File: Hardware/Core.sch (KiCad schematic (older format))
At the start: 24 parts, among them U1 AAT1217

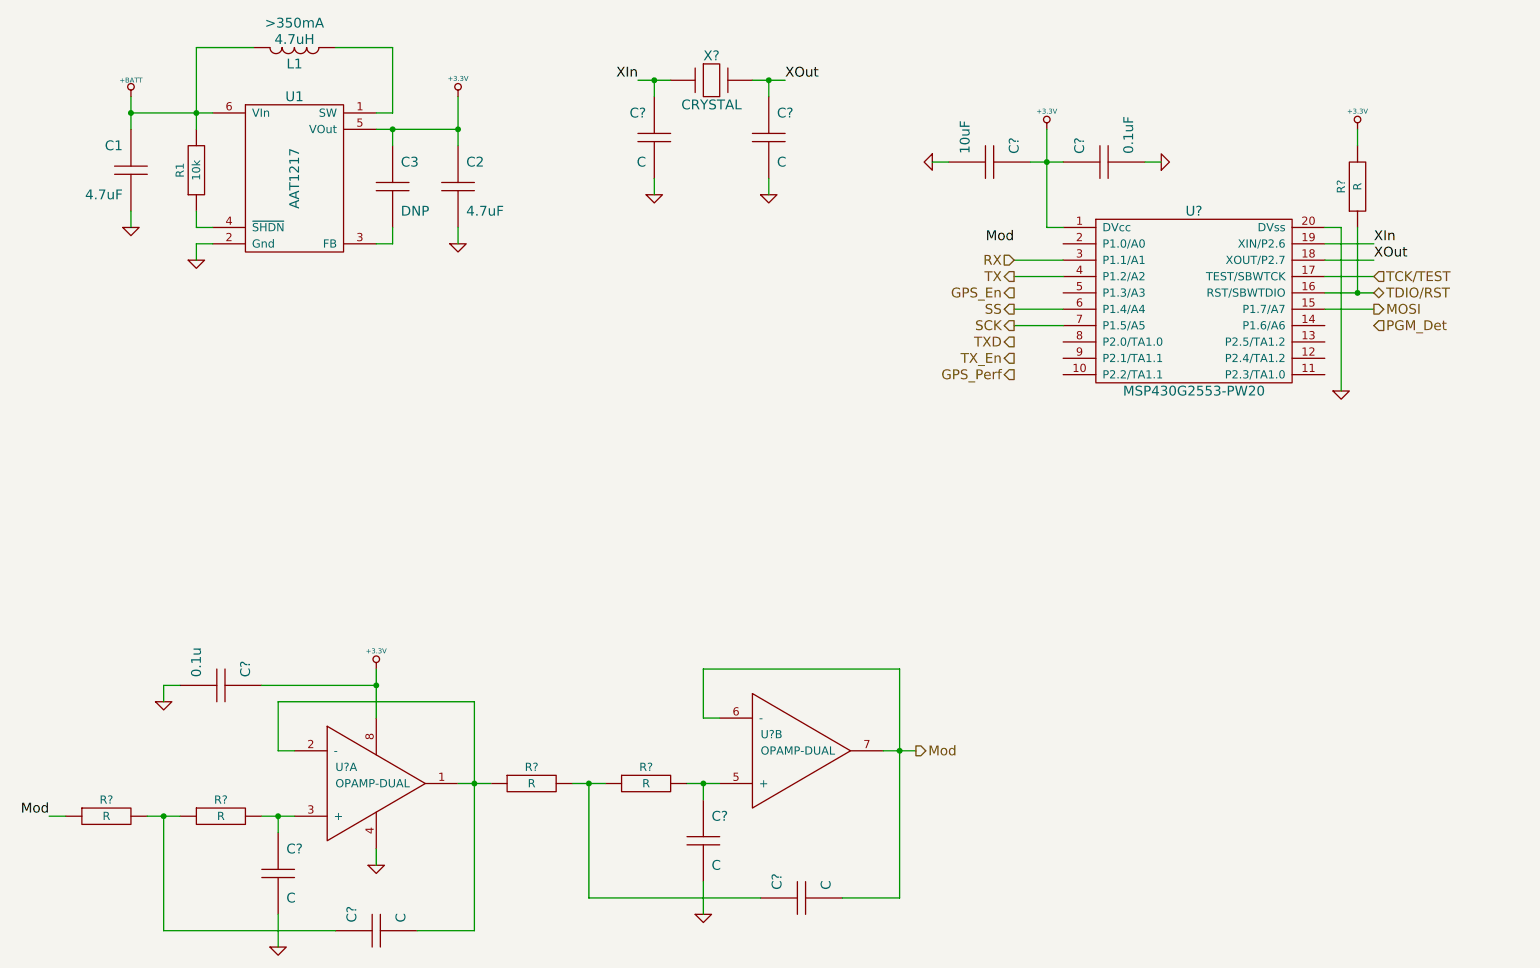
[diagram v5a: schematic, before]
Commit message: Change to 28 pin MCU
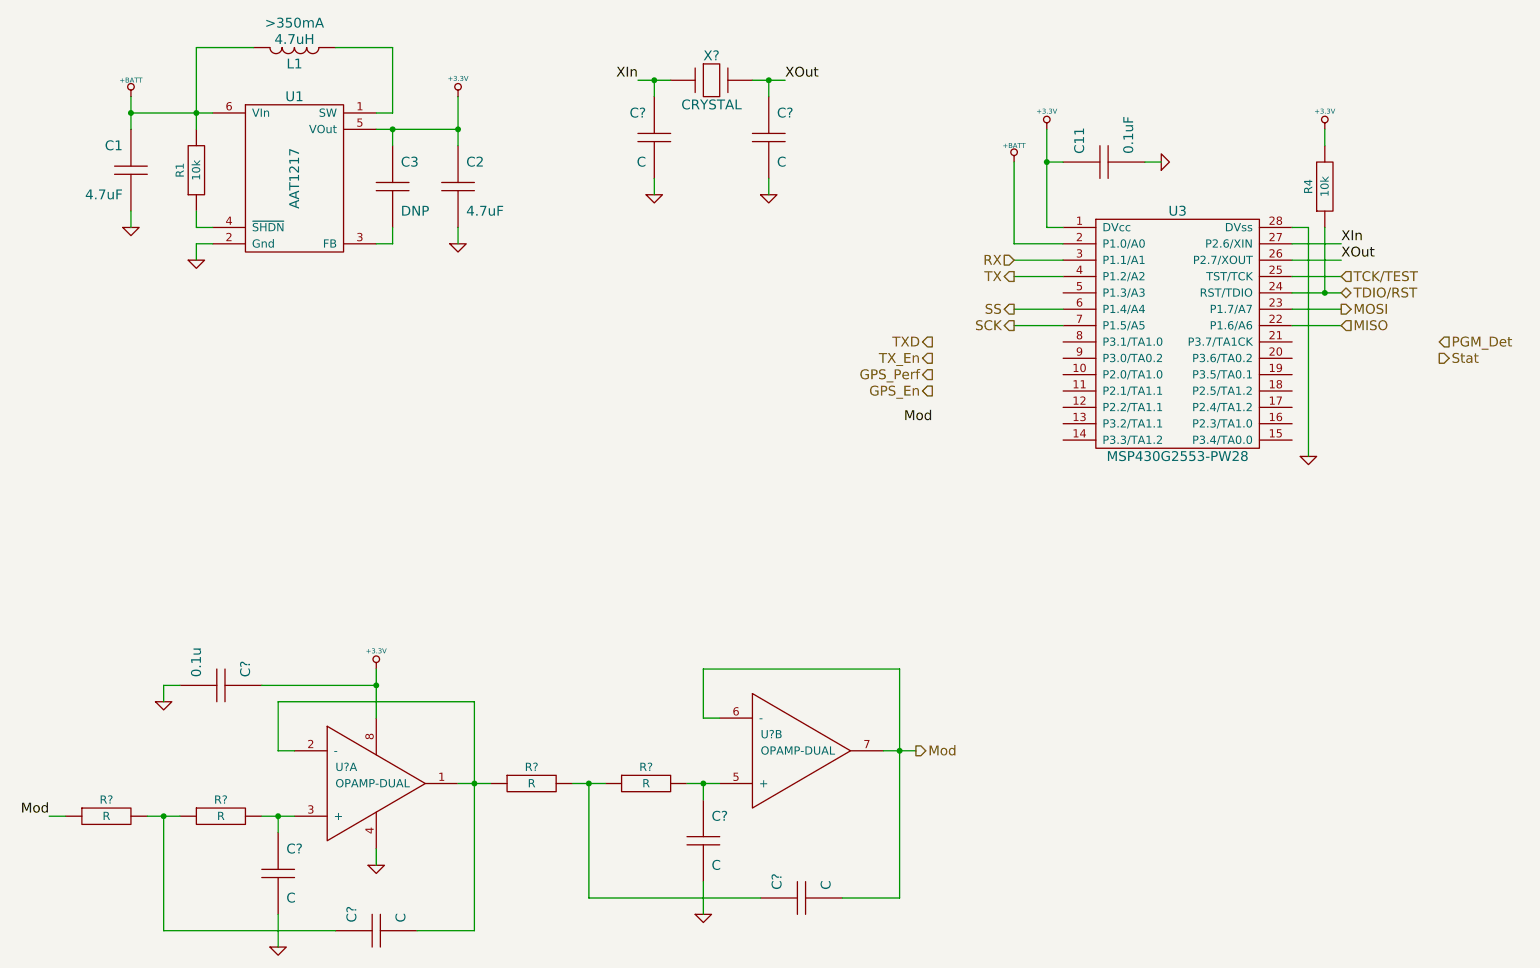
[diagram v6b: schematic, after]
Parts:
- removed C?: 10uF, ~, symbol C
- removed R?: R, ~, symbol R
- removed U?: MSP430G2553-PW20, symbol MSP430G2553-PW20
- added R4: 10k, RESC1608-N, symbol R
- added U3: MSP430G2553-PW28, symbol MSP430G2553-PW28
- C11: renamed from C?; footprint ~ -> CAPC1608-N; Dielectric D -> X7R; Distributor Part No (none) -> 1276-1005-1-ND; MFR Name (none) -> Samsung; MFR Part No (none) -> CL10B104KO8NNNC; Voltage V -> 16V
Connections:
- net +3.3V: now also R4.2, U3.1 (DVcc)
- net +BATT: now also U3.2 (P1.0/A0)
- net GND: now also U3.28 (DVss)
- net MOSI: now also U3.23 (P1.7/A7)
- net RX: now also U3.3 (P1.1/A1)
- net SCK: now also U3.7 (P1.5/A5)
- net SS: now also U3.6 (P1.4/A4)
- net TCK/TEST: now also U3.25 (TST/TCK)
- net TDIO/RST: now also R4.1, U3.24 (RST/TDIO)
- net TX: now also U3.4 (P1.2/A2)
- net XIn: now also U3.27 (P2.6/XIN)
- net XOut: now also U3.26 (P2.7/XOUT)
- new net MISO: U3.22 (P1.6/A6)
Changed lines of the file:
@@
-$EndComp
-$Comp
-L MSP430G2553-PW20 U?
-U 1 1 52ECE44D
-P 8100 3050
-F 0 "U?" H 8100 3600 60  0000 C CNN
-F 1 "MSP430G2553-PW20" H 8100 2500 60  0000 C CNN
-F 2 "" H 8100 3050 60  0000 C CNN
-F 3 "" H 8100 3050 60  0000 C CNN
-	1    8100 3050
-	1    0    0    -1
 $EndComp
 $Comp
 L GND #PWR?
 U 1 1 52ECE5C9
-P 9000 3600
-F 0 "#PWR?" H 9000 3600 30  0001 C CNN
-F 1 "GND" H 9000 3530 30  0001 C CNN
-F 2 "" H 9000 3600 60  0000 C CNN
-F 3 "" H 9000 3600 60  0000 C CNN
-	1    9000 3600
-	1    0    0    -1
-$EndComp
-$Comp
-L R R?
-U 1 1 52ECE61E
-P 9100 2350
-F 0 "R?" H 9100 2450 50  0000 C CNN
-F 1 "R" H 9100 2350 50  0000 C CNN
-F 2 "~" H 9100 2350 60  0000 C CNN
-F 3 "~" H 9100 2350 60  0000 C CNN
-F 4 "W" H 9100 2250 50  0001 C CNN "Power"
-F 5 "%" H 9100 2150 50  0001 C CNN "Tolerance"
-	1    9100 2350
-	0    -1   -1   0
+P 8800 4000
+F 0 "#PWR?" H 8800 4000 30  0001 C CNN
+F 1 "GND" H 8800 3930 30  0001 C CNN
+F 2 "" H 8800 4000 60  0000 C CNN
+F 3 "" H 8800 4000 60  0000 C CNN
+	1    8800 4000
+	1    0    0    -1
 $EndComp
 $Comp
 L +3.3V #PWR?
 U 1 1 52ECE681
-P 9100 2000
-F 0 "#PWR?" H 9100 1960 30  0001 C CNN
-F 1 "+3.3V" H 9100 2110 30  0000 C CNN
-F 2 "" H 9100 2000 60  0000 C CNN
-F 3 "" H 9100 2000 60  0000 C CNN
-	1    9100 2000
+P 8900 2000
+F 0 "#PWR?" H 8900 1960 30  0001 C CNN
+F 1 "+3.3V" H 8900 2110 30  0000 C CNN
+F 2 "" H 8900 2000 60  0000 C CNN
+F 3 "" H 8900 2000 60  0000 C CNN
+	1    8900 2000
 	1    0    0    -1
 $EndComp
@@
 $EndComp
 $Comp
-L C C?
+L C C11
 U 1 1 52ECE6FD
 P 7550 2200
-F 0 "C?" H 7600 2350 60  0000 L CNN
+F 0 "C11" H 7600 2350 60  0000 L CNN
 F 1 "0.1uF" H 7600 2050 60  0000 L CNN
-F 2 "~" H 7550 2200 60  0000 C CNN
+F 2 "CAPC1608-N" H 7550 2200 60  0001 C CNN
 F 3 "~" H 7550 2200 60  0000 C CNN
-F 4 "V" H 7500 2050 60  0001 R CNN "Voltage"
-F 5 "D" H 7500 2350 60  0001 R CNN "Dielectric"
+F 4 "Samsung" H 7550 2200 60  0001 C CNN "MFR Name"
+F 5 "CL10B104KO8NNNC" H 7550 2200 60  0001 C CNN "MFR Part No"
+F 6 "1276-1005-1-ND" H 7550 2200 60  0001 C CNN "Distributor Part No"
+F 7 "16V" H 7500 2050 60  0001 R CNN "Voltage"
+F 8 "X7R" H 7500 2350 60  0001 R CNN "Dielectric"
 	1    7550 2200
 	0    -1   -1   0
-$EndComp
-$Comp
-L C C?
-U 1 1 52ECE724
-P 6850 2200
-F 0 "C?" H 6900 2350 60  0000 L CNN
-F 1 "10uF" H 6900 2050 60  0000 L CNN
-F 2 "~" H 6850 2200 60  0000 C CNN
-F 3 "~" H 6850 2200 60  0000 C CNN
-F 4 "V" H 6800 2050 60  0001 R CNN "Voltage"
-F 5 "D" H 6800 2350 60  0001 R CNN "Dielectric"
-	1    6850 2200
-	0    1    -1   0
-$EndComp
-$Comp
-L GND #PWR?
-U 1 1 52ECE733
-P 6500 2200
-F 0 "#PWR?" H 6500 2200 30  0001 C CNN
-F 1 "GND" H 6500 2130 30  0001 C CNN
-F 2 "" H 6500 2200 60  0000 C CNN
-F 3 "" H 6500 2200 60  0000 C CNN
-	1    6500 2200
-	0    1    1    0
 $EndComp
 $Comp
@@
 Text HLabel 7000 2900 0    60   Output ~ 0
 TX
-Text HLabel 7000 3000 0    60   Output ~ 0
+Text HLabel 6500 3600 0    60   Output ~ 0
 GPS_En
-Text HLabel 9200 3100 2    60   Output ~ 0
+Text HLabel 9000 3100 2    60   Output ~ 0
 MOSI
 Text HLabel 7000 3200 0    60   Output ~ 0
@@
 Text HLabel 7000 3100 0    60   Output ~ 0
 SS
-Text HLabel 7000 3400 0    60   Output ~ 0
+Text HLabel 6500 3400 0    60   Output ~ 0
 TX_En
-Text HLabel 7000 3300 0    60   Output ~ 0
+Text HLabel 6500 3300 0    60   Output ~ 0
 TXD
 Text HLabel 6400 5800 2    60   Output ~ 0
 Mod
-Text HLabel 9200 3000 2    60   BiDi ~ 0
+Text HLabel 9000 3000 2    60   BiDi ~ 0
 TDIO/RST
-Text HLabel 9200 2900 2    60   Input ~ 0
+Text HLabel 9000 2900 2    60   Input ~ 0
 TCK/TEST
-Text HLabel 9200 3200 2    60   Input ~ 0
+Text HLabel 9600 3300 2    60   Input ~ 0
 PGM_Det
 $Comp
@@
 	2000 2600 2100 2600
 Wire Wire Line
-	1600 1800 1600 1900
-Wire Wire Line
-	1600 1900 1600 2000
-Wire Wire Line
-	1600 1900 2000 1900
-Wire Wire Line
-	2000 1900 2100 1900
+	1600 1800 1600 2000
+Wire Wire Line
+	1600 1900 2100 1900
 Connection ~ 1600 1900
 Wire Wire Line
-	2000 1500 2000 1900
-Wire Wire Line
-	2000 1900 2000 2000
+	2000 1500 2000 2000
 Connection ~ 2000 1900
 Wire Wire Line
 	2000 1500 2350 1500
 Wire Wire Line
-	3100 2000 3200 2000
-Wire Wire Line
-	3200 2000 3600 2000
-Wire Wire Line
-	3600 1800 3600 2000
-Wire Wire Line
-	3600 2000 3600 2100
+	3100 2000 3600 2000
+Wire Wire Line
+	3600 1800 3600 2100
 Wire Wire Line
 	2000 2800 2000 2700
@@
 Connection ~ 3600 2000
 Wire Wire Line
-	9000 3600 9000 2600
-Wire Wire Line
-	9000 2600 8900 2600
-Wire Wire Line
-	8900 2900 9200 2900
-Wire Wire Line
-	8900 3000 9100 3000
-Wire Wire Line
-	9100 3000 9200 3000
-Wire Wire Line
-	9100 2600 9100 3000
-Connection ~ 9100 3000
-Wire Wire Line
-	9100 2000 9100 2100
-Wire Wire Line
-	7200 2000 7200 2200
-Wire Wire Line
-	7200 2200 7200 2600
+	8800 4000 8800 2600
+Wire Wire Line
+	8800 2600 8700 2600
+Wire Wire Line
+	8700 2900 9000 2900
+Wire Wire Line
+	8700 3000 9000 3000
+Wire Wire Line
+	8900 2600 8900 3000
+Connection ~ 8900 3000
+Wire Wire Line
+	8900 2000 8900 2100
+Wire Wire Line
+	7200 2000 7200 2600
 Wire Wire Line
 	7200 2600 7300 2600
 Wire Wire Line
 	7900 2200 7800 2200
-Wire Wire Line
-	6500 2200 6600 2200
-Wire Wire Line
-	7100 2200 7200 2200
-Wire Wire Line
-	7200 2200 7300 2200
 Connection ~ 7200 2200
 Wire Wire Line
@@
 	7000 2900 7300 2900
 Wire Wire Line
-	9200 3100 8900 3100
+	9000 3100 8700 3100
 Wire Wire Line
 	7000 3100 7300 3100
@@
 	2500 6800 2500 7000
 Wire Wire Line
-	1700 6200 1800 6200
-Wire Wire Line
-	1800 6200 1900 6200
+	1700 6200 1900 6200
 Wire Wire Line
 	1800 6200 1800 6900
 Wire Wire Line
-	3700 5500 3700 6000
-Wire Wire Line
-	3700 6000 3700 6900
-Wire Wire Line
-	3600 6000 3700 6000
-Wire Wire Line
-	3700 6000 3800 6000
+	3700 5500 3700 6900
+Wire Wire Line
+	3600 6000 3800 6000
 Connection ~ 1800 6200
 Wire Wire Line
@@
 	3100 6400 3100 6500
 Wire Wire Line
-	2400 6200 2500 6200
-Wire Wire Line
-	2500 6200 2600 6200
+	2400 6200 2600 6200
 Wire Wire Line
 	2500 6300 2500 6200
@@
 	3700 6900 3350 6900
 Wire Wire Line
-	4300 6000 4400 6000
-Wire Wire Line
-	4400 6000 4500 6000
-Wire Wire Line
-	5000 6000 5100 6000
-Wire Wire Line
-	5100 6000 5200 6000
+	4300 6000 4500 6000
+Wire Wire Line
+	5000 6000 5200 6000
 Wire Wire Line
 	5100 6100 5100 6000
@@
 	5100 5300 6300 5300
 Wire Wire Line
-	6300 5300 6300 5800
-Wire Wire Line
-	6300 5800 6300 6700
-Wire Wire Line
-	6200 5800 6300 5800
-Wire Wire Line
-	6300 5800 6400 5800
+	6300 5300 6300 6700
+Wire Wire Line
+	6200 5800 6400 5800
 Wire Wire Line
 	6300 6700 5950 6700
@@
 $EndComp
 Wire Wire Line
-	3100 5300 3100 5400
-Wire Wire Line
-	3100 5400 3100 5600
+	3100 5300 3100 5600
 Wire Wire Line
 	2400 5400 3100 5400
@@
 Wire Wire Line
 	1100 6200 1200 6200
-Text Label 7000 2700 2    60   ~ 0
+Text Label 6500 3800 2    60   ~ 0
 Mod
-Text HLabel 7000 3500 0    60   Output ~ 0
+Text HLabel 6500 3500 0    60   Output ~ 0
 GPS_Perf
 $Comp
@@
 XIn
 Wire Wire Line
-	4700 1700 4800 1700
-Wire Wire Line
-	4800 1700 4900 1700
-Wire Wire Line
-	5400 1700 5500 1700
-Wire Wire Line
-	5500 1700 5600 1700
+	4700 1700 4900 1700
+Wire Wire Line
+	5400 1700 5600 1700
 Wire Wire Line
 	5500 1800 5500 1700
@@
 Wire Wire Line
 	5500 2300 5500 2400
-Text Label 9200 2700 0    60   ~ 0
+Text Label 9000 2700 0    60   ~ 0
 XIn
-Text Label 9200 2800 0    60   ~ 0
+Text Label 9000 2800 0    60   ~ 0
 XOut
 Wire Wire Line
-	8900 2700 9200 2700
-Wire Wire Line
-	8900 2800 9200 2800
+	8700 2700 9000 2700
+Wire Wire Line
+	8700 2800 9000 2800
 $Comp
 L C C3
@@
 	1    0    0    -1
 $EndComp
+Text HLabel 9000 3200 2    60   Input ~ 0
+MISO
+Wire Wire Line
+	9000 3200 8700 3200
+$Comp
+L R R4
+U 1 1 52EF83E3
+P 8900 2350
+F 0 "R4" H 8900 2450 50  0000 C CNN
+F 1 "10k" H 8900 2350 50  0000 C CNN
+F 2 "RESC1608-N" H 8900 2350 60  0001 C CNN
+F 3 "~" H 8900 2350 60  0000 C CNN
+F 4 "Yageo" H 8900 2350 60  0001 C CNN "MFR Name"
+F 5 "RC0603JR-0710KL" H 8900 2350 60  0001 C CNN "MFR Part No"
+F 6 "311-10KGRCT-ND" H 8900 2350 60  0001 C CNN "Distributor Part No"
+F 7 "0.1W" H 8900 2250 50  0001 C CNN "Power"
+F 8 "5%" H 8900 2150 50  0001 C CNN "Tolerance"
+	1    8900 2350
+	0    -1   -1   0
+$EndComp
+Wire Wire Line
+	7200 2200 7300 2200
+$Comp
+L MSP430G2553-PW28 U3
+U 1 1 52EFA4DC
+P 8000 3250
+F 0 "U3" H 8000 4000 60  0000 C CNN
+F 1 "MSP430G2553-PW28" H 8000 2500 60  0000 C CNN
+F 2 "" H 8000 2400 60  0000 C CNN
+F 3 "" H 8000 2400 60  0000 C CNN
+F 4 "TI" H 8000 3250 60  0001 C CNN "MFR Name"
+F 5 "MSP430G2553IPW28R" H 8000 3250 60  0001 C CNN "MFR Part No"
+F 6 "296-28431-1-ND" H 8000 3250 60  0001 C CNN "Distributor Part No"
+	1    8000 3250
+	1    0    0    -1
+$EndComp
+Text HLabel 9600 3400 2    60   Output ~ 0
+Stat
+$Comp
+L +BATT #PWR?
+U 1 1 52EFA84C
+P 7000 2200
+F 0 "#PWR?" H 7000 2150 20  0001 C CNN
+F 1 "+BATT" H 7000 2300 30  0000 C CNN
+F 2 "" H 7000 2200 60  0000 C CNN
+F 3 "" H 7000 2200 60  0000 C CNN
+	1    7000 2200
+	1    0    0    -1
+$EndComp
+Wire Wire Line
+	7000 2200 7000 2700
+Wire Wire Line
+	7000 2700 7300 2700
 $EndSCHEMATC

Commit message: Modulation section values
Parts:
- removed C? (x4): C, ~, symbol C
- removed C?: 0.1u, ~, symbol C
- removed R? (x3): R, ~, symbol R
- removed U?: OPAMP-DUAL, ~, symbol OPAMP-DUAL
- added C12, C13, C14, C15: 1000pF, CAPC1608-N, symbol C
- added C12: 0.1uF, CAPC1608-N, symbol C
- added R6, R7, R8: 16k, RESC1608-N, symbol R
- added unit 2 of U4
- R5: renamed from R?; value R -> 16k; footprint ~ -> RESC1608-N; Distributor Part No (none) -> 311-16.0KHRCT-ND; MFR Name (none) -> Yageo; MFR Part No (none) -> RC0603FR-0716KL; Power W -> 0.1W; Tolerance % -> 1%
- U4: renamed from U?; value OPAMP-DUAL -> MCP6L02T; footprint ~ -> SOP65P490-8N; Distributor Part No (none) -> MCP6L02T-E/MSCT-ND; MFR Name (none) -> Microchip; MFR Part No (none) -> MCP6L02T-E/MS
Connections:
- net +3.3V: now also C12.1
- net GND: now also C12.2, C13.2, C15.2
- net Mod: now also C14.2, U4.6 (-), U4.7
- net at U4.1, U4.2 (-): now also C12.2, R7.1
- net at U4.3 (+): now also C13.1, R6.2
- net at R5.2: now also C12.1, R6.1
- net MISO renamed SCL
- net MOSI renamed DATA
- new net: C15.1, R8.2, U4.5 (+)
- new net: C14.1, R7.2, R8.1
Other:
- note added: "Butterworth LPF"
